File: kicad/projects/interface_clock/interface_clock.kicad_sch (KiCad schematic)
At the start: 74 parts, among them J1 Control_signal_backplane, J10 Power, J2 Aux_connection, J3 Bus_connection, J4 ADDRESS IN, J5 EXT BUS AND ADDR, J7 CTL SIGS, J9 LED CTL, U1 74HC02, U10 74HC157, U11 74HC14, U12 74HC245, U13 74HC126, U14 74HC109, U2 74HC04, U3 74HC08, U5 74HC02, U6 74HC245, U7 74HC245, U8 74HC245, U9 74HC245, X1 CXO_DIP8

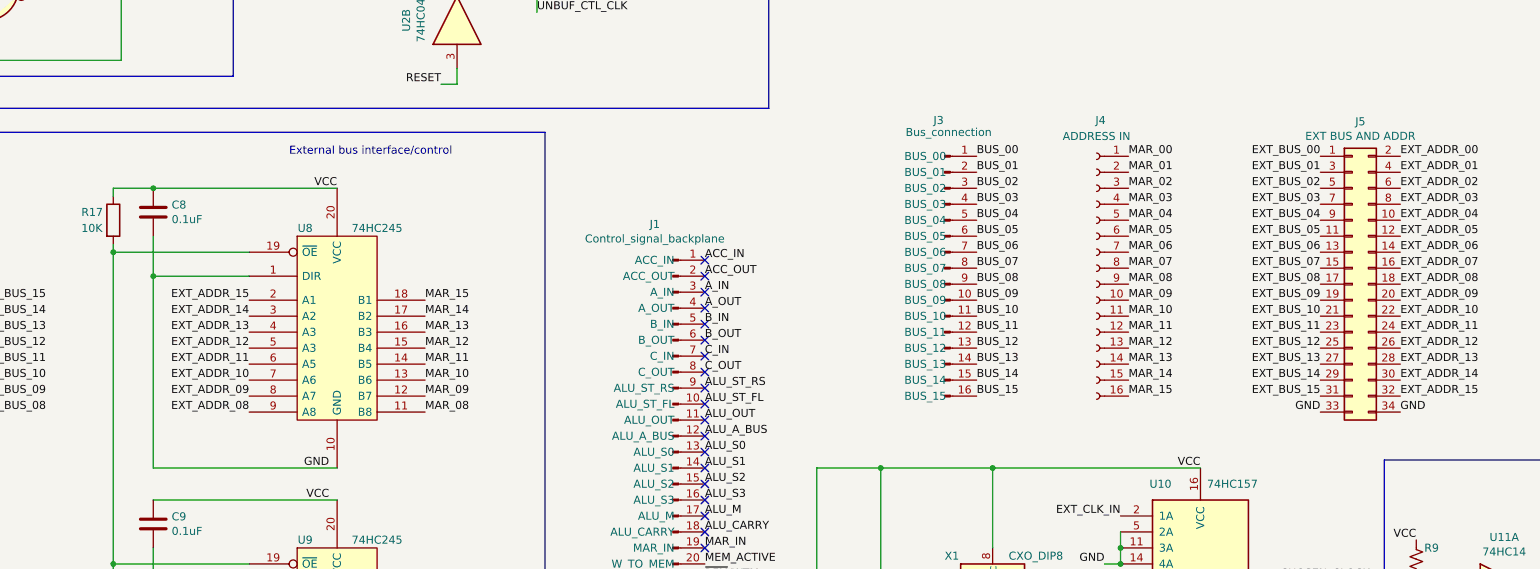
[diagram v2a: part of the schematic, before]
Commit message: Interface clock bus connector updated.
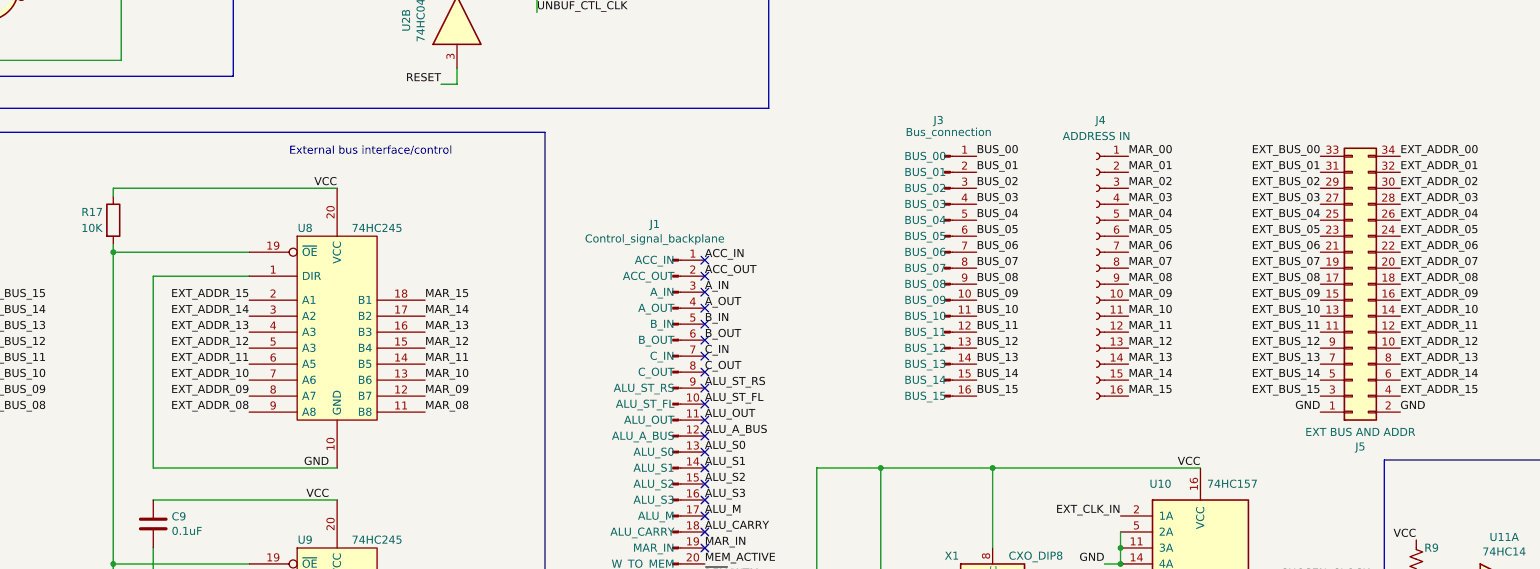
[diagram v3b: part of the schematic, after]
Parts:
- removed C8: 0.1uF, Capacitor_THT:C_Disc_D4.7mm_W2.5mm_P5.00mm, symbol Device:C
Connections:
- net EXT_ADDR_00: now also J5.34 (Pin_34); no longer J5.2 (Pin_2)
- net EXT_ADDR_01: now also J5.32 (Pin_32); no longer J5.4 (Pin_4)
- net EXT_ADDR_02: now also J5.30 (Pin_30); no longer J5.6 (Pin_6)
- net EXT_ADDR_03: now also J5.28 (Pin_28); no longer J5.8 (Pin_8)
- net EXT_ADDR_04: now also J5.26 (Pin_26); no longer J5.10 (Pin_10)
- net EXT_ADDR_05: now also J5.24 (Pin_24); no longer J5.12 (Pin_12)
- net EXT_ADDR_06: now also J5.22 (Pin_22); no longer J5.14 (Pin_14)
- net EXT_ADDR_07: now also J5.20 (Pin_20); no longer J5.16 (Pin_16)
- net EXT_ADDR_09: now also J5.16 (Pin_16); no longer J5.20 (Pin_20)
- net EXT_ADDR_10: now also J5.14 (Pin_14); no longer J5.22 (Pin_22)
- net EXT_ADDR_11: now also J5.12 (Pin_12); no longer J5.24 (Pin_24)
- net EXT_ADDR_12: now also J5.10 (Pin_10); no longer J5.26 (Pin_26)
- net EXT_ADDR_13: now also J5.8 (Pin_8); no longer J5.28 (Pin_28)
- net EXT_ADDR_14: now also J5.6 (Pin_6); no longer J5.30 (Pin_30)
- net EXT_ADDR_15: now also J5.4 (Pin_4); no longer J5.32 (Pin_32)
- net EXT_BUS_00: now also J5.33 (Pin_33); no longer J5.1 (Pin_1)
- net EXT_BUS_01: now also J5.31 (Pin_31); no longer J5.3 (Pin_3)
- net EXT_BUS_02: now also J5.29 (Pin_29); no longer J5.5 (Pin_5)
- net EXT_BUS_03: now also J5.27 (Pin_27); no longer J5.7 (Pin_7)
- net EXT_BUS_04: now also J5.25 (Pin_25); no longer J5.9 (Pin_9)
- net EXT_BUS_05: now also J5.23 (Pin_23); no longer J5.11 (Pin_11)
- net EXT_BUS_06: now also J5.21 (Pin_21); no longer J5.13 (Pin_13)
- net EXT_BUS_07: now also J5.19 (Pin_19); no longer J5.15 (Pin_15)
- net EXT_BUS_09: now also J5.15 (Pin_15); no longer J5.19 (Pin_19)
- net EXT_BUS_10: now also J5.13 (Pin_13); no longer J5.21 (Pin_21)
- net EXT_BUS_11: now also J5.11 (Pin_11); no longer J5.23 (Pin_23)
- net EXT_BUS_12: now also J5.9 (Pin_9); no longer J5.25 (Pin_25)
- net EXT_BUS_13: now also J5.7 (Pin_7); no longer J5.27 (Pin_27)
- net EXT_BUS_14: now also J5.5 (Pin_5); no longer J5.29 (Pin_29)
- net EXT_BUS_15: now also J5.3 (Pin_3); no longer J5.31 (Pin_31)
- net GND: now also J5.1 (Pin_1), J5.2 (Pin_2); no longer J5.33 (Pin_33), J5.34 (Pin_34)
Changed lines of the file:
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@@
   (junction (at 55.88 199.39) (diameter 0) (color 0 0 0 0)
   )
-  (junction (at 151.13 101.6) (diameter 0) (color 0 0 0 0)
-  )
   (junction (at 520.7 233.68) (diameter 0) (color 0 0 0 0)
   )
@@
   (junction (at 226.06 199.39) (diameter 0) (color 0 0 0 0)
   )
-  (junction (at 151.13 87.63) (diameter 0) (color 0 0 0 0)
-  )
   (junction (at 486.41 214.63) (diameter 0) (color 0 0 0 0)
   )
@@
     (stroke (width 0) (type default))
   )
-  (wire (pts (xy 151.13 87.63) (xy 180.34 87.63))
+  (wire (pts (xy 144.78 87.63) (xy 180.34 87.63))
     (stroke (width 0) (type default))
   )
@@
     (stroke (width 0) (type default))
   )
-  (wire (pts (xy 144.78 87.63) (xy 151.13 87.63))
-    (stroke (width 0) (type default))
-  )
   (wire (pts (xy 520.7 241.3) (xy 520.7 237.49))
     (stroke (width 0) (type default))
@@
     (stroke (width 0) (type default))
   )
-  (wire (pts (xy 151.13 95.25) (xy 151.13 101.6))
-    (stroke (width 0) (type default))
-  )
   (wire (pts (xy 210.82 224.79) (xy 196.85 224.79))
     (stroke (width 0) (type default))
@@
     )
   )
-  (symbol (lib_id "Device:C") (at 151.13 91.44 0) (unit 1)
-    (in_bom yes) (on_board yes) (dnp no)
-    (property "Reference" "C8" (at 154.051 90.2716 0)
-      (effects (font (size 1.27 1.27)) (justify left))
-    )
-    (property "Value" "0.1uF" (at 154.051 92.583 0)
-      (effects (font (size 1.27 1.27)) (justify left))
-    )
-    (property "Footprint" "Capacitor_THT:C_Disc_D4.7mm_W2.5mm_P5.00mm" (at 152.0952 95.25 0)
-      (effects (font (size 1.27 1.27)) hide)
-    )
-    (property "Datasheet" "~" (at 151.13 91.44 0)
-      (effects (font (size 1.27 1.27)) hide)
-    )
-    (pin "1")
-    (pin "2")
-    (instances
-      (project "interface_clock"
-        (path "/b59c01df-13a6-441a-94e3-57cb7ed09942"
-          (reference "C8") (unit 1)
-        )
-      )
-    )
-  )
   (symbol (lib_id "Device:C") (at 153.67 212.09 0) (unit 1)
     (in_bom yes) (on_board yes) (dnp no)
@@
     )
   )
-  (symbol (lib_id "Connector_Generic:Conn_02x17_Odd_Even") (at 341.63 102.87 0) (unit 1)
+  (symbol (lib_id "Connector_Generic:Conn_02x17_Odd_Even") (at 341.63 102.87 0) (mirror x) (unit 1)
     (in_bom yes) (on_board yes) (dnp no)
-    (property "Reference" "J5" (at 342.9 77.0382 0)
+    (property "Reference" "J5" (at 342.9 128.7018 0)
       (effects (font (size 1.27 1.27)))
     )
-    (property "Value" "EXT BUS AND ADDR" (at 342.9 79.3496 0)
+    (property "Value" "EXT BUS AND ADDR" (at 342.9 126.3904 0)
       (effects (font (size 1.27 1.27)))
     )

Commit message: Tech checks on interface clock complete.
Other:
- note added: "Inputs"
- note added: "Outputs"
- note added: "This makes sure that before reset goes high, the clock is disabled, then after the reset goes low, the clock is re enabled."
- note removed: "Reset signal disabling clock"
- moved on the sheet: C15, C16, C19, D1, D2, D3, D4, D5, D6, D7, D8, R1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
